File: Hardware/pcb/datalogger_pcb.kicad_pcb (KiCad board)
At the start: 2 copper layers, 127.5 x 123.3 mm, 51 parts, among them J1 Micro_SD_Card_Det2, J2 Switch OUT, SW1 SW_Wuerth_450301014042, SW2 SW_Push, U1 DS3231MZ, U2 SN74LVC2G00DCTR

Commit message: Improvements to PCB and code
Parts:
- 10k: renamed from Pullup CS
- moved 10k 24.2 mm to (156.2, 71.5)
- moved BT1 6.85 mm to (146.7, 95.5)
- moved C4 6.00 mm to (158.5, 82.3)
- moved R5 5.79 mm to (152.2, 84.6), turned to 0 degrees
- moved Rpllup1 2.23 mm to (143.6, 79.0)
- moved Rpllup2 2.10 mm to (147.7, 84.6)
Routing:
- net /Batt+: track 28.3 -> 24.0 mm
- net +3.3V: track 425.5 -> 427.9 mm
- net /I2C0_SCL: track 164.4 -> 162.3 mm
- net Net-(A1-GPIO21): track 130.4 -> 132.2 mm
- net /Data_Onewire: track 95.9 -> 97.2 mm
- net /CS: track 82.1 -> 81.2 mm

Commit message: Small changes
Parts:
- removed RpullupSCL0, RpullupSDA0: 10k, Resistor_THT:R_Axial_DIN0204_L3.6mm_D1.6mm_P5.08mm_Vertical
- renumbered 12V to 12VSWTCH1, 5V to 5VSWTCH1, 10k to RpullupCS1
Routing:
- net /I2C0_SCL: track 162.3 -> 148.3 mm, vias 2 -> 1
- net +3.3V: track 427.9 -> 416.4 mm
- net /I2C0_SDA: track 174.6 -> 170.8 mm

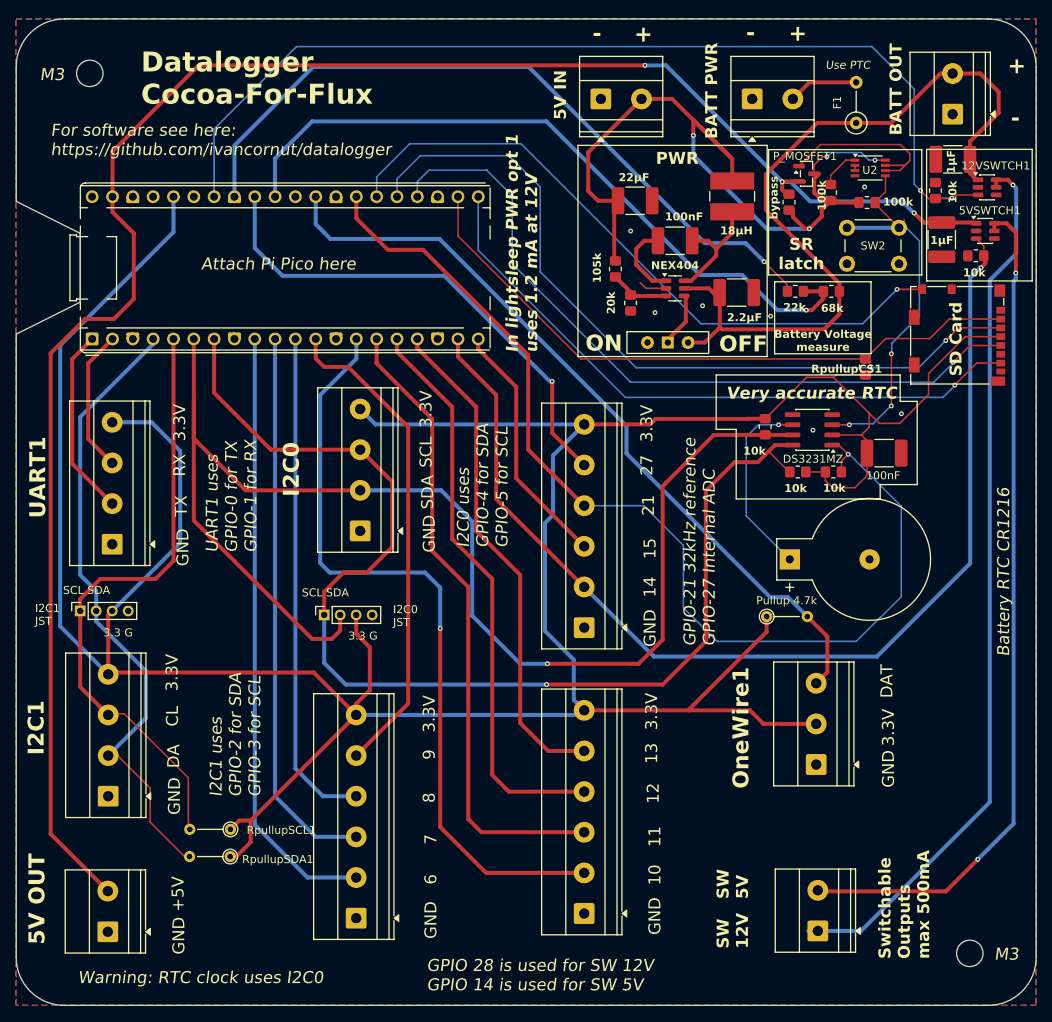
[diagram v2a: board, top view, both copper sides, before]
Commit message: Improved datalogger design and reduced pcb size
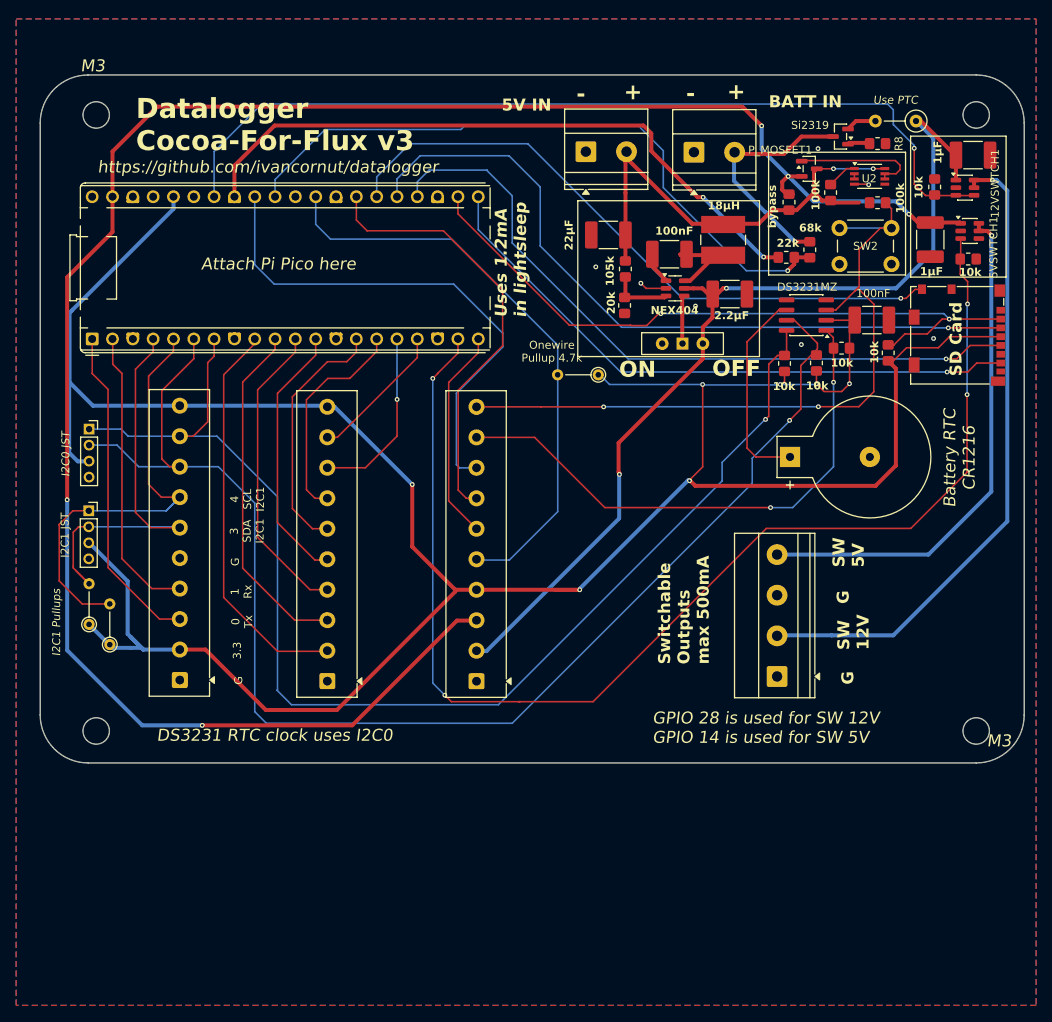
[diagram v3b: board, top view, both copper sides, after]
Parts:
- removed 5VPOUT1: Bornier 5V, TerminalBlock_Phoenix:TerminalBlock_Phoenix_MKDS-1,5-2-5.08_1x02_P5.08mm_Horizontal
- removed GPIO10-1: GPIO10-13, TerminalBlock_Phoenix:TerminalBlock_Phoenix_MKDS-1,5-6-5.08_1x06_P5.08mm_Horizontal
- removed GPIO14-1: GPIO14-17, TerminalBlock_Phoenix:TerminalBlock_Phoenix_MKDS-1,5-6-5.08_1x06_P5.08mm_Horizontal
- removed GPIO6-1: GPIO6-9, TerminalBlock_Phoenix:TerminalBlock_Phoenix_MKDS-1,5-6-5.08_1x06_P5.08mm_Horizontal
- removed I2C0JST1: I2C 0 Connector, Connector_PinSocket_2.00mm:PinSocket_1x04_P2.00mm_Vertical
- removed I2C1: I2C 1 Connector, TerminalBlock_Phoenix:TerminalBlock_Phoenix_MKDS-1,5-4-5.08_1x04_P5.08mm_Horizontal
- removed I2C1JST1: I2C 1 Connector, Connector_PinSocket_2.00mm:PinSocket_1x04_P2.00mm_Vertical
- removed I2C2: I2C 0 Connector, TerminalBlock_Phoenix:TerminalBlock_Phoenix_MKDS-1,5-4-5.08_1x04_P5.08mm_Horizontal
- removed J2: Switch OUT, TerminalBlock_Phoenix:TerminalBlock_Phoenix_MKDS-1,5-2-5.08_1x02_P5.08mm_Horizontal
- removed OneWire1: Connecteur OneWire, TerminalBlock_Phoenix:TerminalBlock_Phoenix_MKDS-1,5-3-5.08_1x03_P5.08mm_Horizontal
- removed PWR12V1: 12V PWR, TerminalBlock_Phoenix:TerminalBlock_Phoenix_MKDS-1,5-2-5.08_1x02_P5.08mm_Horizontal
- removed UART1: UART Connector, TerminalBlock_Phoenix:TerminalBlock_Phoenix_MKDS-1,5-4-5.08_1x04_P5.08mm_Horizontal
- added I2C0 JST: I2C 0 Connector, Connector_PinSocket_2.00mm:PinSocket_1x04_P2.00mm_Vertical, F.Cu at (59.1, 79.3)
- added I2C1 JST: I2C 1 Connector, Connector_PinSocket_2.00mm:PinSocket_1x04_P2.00mm_Vertical, F.Cu at (59.1, 89.5)
- added J3: Conn_01x10_Socket, TerminalBlock_Phoenix:TerminalBlock_Phoenix_MKDS-1-10-3.81_1x10_P3.81mm_Horizontal, F.Cu at (88.9, 110.8)
- added J4: Conn_01x10_Socket, TerminalBlock_Phoenix:TerminalBlock_Phoenix_MKDS-1-10-3.81_1x10_P3.81mm_Horizontal, F.Cu at (107.5, 110.8)
- added J5: Conn_01x10_Socket, TerminalBlock_Phoenix:TerminalBlock_Phoenix_MKDS-1-10-3.81_1x10_P3.81mm_Horizontal, F.Cu at (70.5, 110.6)
- added J6: Conn_01x04_Socket, TerminalBlock_Phoenix:TerminalBlock_Phoenix_MKDS-1,5-4-5.08_1x04_P5.08mm_Horizontal, F.Cu at (145.1, 110.2)
- added Q1: Si2319CDS, Package_TO_SOT_SMD:SOT-23, F.Cu at (153.0, 42.7)
- added R8: 100k, Resistor_SMD:R_0805_2012Metric_Pad1.20x1.40mm_HandSolder, F.Cu at (157.7, 43.6)
- moved Pullup_One_Wire1 36.8 mm to (122.8, 72.5), turned to 180 degrees
- moved RpullupSDA1 34.0 mm to (59.1, 103.7), turned to 90 degrees
- moved RpullupSCL1 27.6 mm to (61.7, 106.2), turned to 90 degrees
- moved C4 16.7 mm to (157.0, 65.6)
- moved R5 15.5 mm to (153.2, 69.2), turned to 180 degrees
- moved U1 14.4 mm to (148.8, 65.0)
- moved Rpllup2 13.7 mm to (146.0, 71.1), turned to 90 degrees
- moved BT1 12.8 mm to (146.7, 82.8)
- moved Rpllup1 10.2 mm to (150.0, 71.0), turned to 90 degrees
- moved PWRIN1 9.87 mm to (134.7, 44.7)
- moved F1 7.48 mm to (162.5, 40.8), turned to 180 degrees
- moved Alim5V1 6.85 mm to (121.2, 44.6)
- moved R1 5.86 mm to (149.2, 56.9), turned to -90 degrees
- moved L_alim1 5.56 mm to (138.4, 55.6)
- moved C3 5.43 mm to (124.0, 55.0), turned to 180 degrees
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- renumbered RpullupCS1 to 10k
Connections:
- F1 pad 2: Net-(PWRIN1-Pin_2) -> Net-(Q1-S)
- PWRIN1 pad 2: Net-(PWRIN1-Pin_2) -> /BATTREAD
- R1 pad 1: +12V -> /BATTREAD
- R5 pad 2: Net-(A1-GPIO21) -> Net-(J4-Pin_9)
- U1 pad 1: Net-(A1-GPIO21) -> Net-(J4-Pin_9)
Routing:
- net +3.3V: track 416.4 -> 334.3 mm, vias 0 -> 7
- net Net-(A1-GPIO21): track 132.2 -> 54.9 mm, vias 1 -> 0
- net Net-(J4-Pin_9): track 0.00 -> 67.8 mm, vias 0 -> 2
- net Net-(A1-GPIO10): track 96.4 -> 31.3 mm, vias 1 -> 0
- net Net-(A1-GPIO11): track 80.0 -> 28.7 mm
- net Net-(A1-GPIO12): track 71.8 -> 22.5 mm, vias 0 -> 1
- net Net-(A1-GPIO13): track 62.8 -> 17.8 mm
- net Net-(5VSWTCH1-QOD): track 106.4 -> 64.9 mm, vias 2 -> 1
- net /RTC_INT: track 48.8 -> 90.0 mm, vias 3 -> 2
- net +5V: track 101.2 -> 61.7 mm, vias 4 -> 2
- net Net-(12VSWTCH1-QOD): track 111.4 -> 81.8 mm
- net /BATTREAD: track 0.00 -> 29.5 mm, vias 0 -> 1
- net Net-(A1-GPIO9): track 61.3 -> 33.2 mm
- net /I2C1_SDA: track 79.5 -> 53.0 mm
- net Net-(A1-GPIO6): track 76.1 -> 49.7 mm
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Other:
- board size 127.5 x 123.3 mm -> 123 x 86 mm
- board text added: "0 Tx"
- board text added: "1 Rx"
- board text added: "3 SDA I2C1"
- board text added: "3.3"
- board text added: "4 SCL I2C1"
- board text added: "BATT IN"
- board text added: "DS3231 RTC clock uses I2C0"
- board text added: "Datalogger Cocoa-For-Flux v3"
- board text added: "G"
- board text added: "I2C1 Pullups"
- board text added: "Onewire Pullup 4.7k"
- board text added: "Si2319"
- board text added: "Uses 1.2mA in lightsleep"
- board text added: "https://github.com/ivancornut/datalogger"
- board text removed: "+5V"
- board text removed: "10"
- board text removed: "11"
- board text removed: "12"
- board text removed: "13"
- board text removed: "14"
- board text removed: "15"
- board text removed: "21"
- board text removed: "27"
- board text removed: "3.3 G"
- board text removed: "3.3V"
- board text removed: "5V OUT"
- board text removed: "6"
- board text removed: "7"
- board text removed: "8"
- board text removed: "9"
- board text removed: "BATT OUT"
- board text removed: "BATT PWR"
- board text removed: "Battery Voltage measure"
- board text removed: "CL"
- board text removed: "DA"
- board text removed: "DAT"
- board text removed: "Datalogger Cocoa-For-Flux"
- board text removed: "For software see here: https://github.com/ivancornut/datalogger"
- board text removed: "GND"
- board text removed: "GPIO-21 32kHz reference GPIO-27 Internal ADC"
- board text removed: "I2C0"
- board text removed: "I2C0 JST"
- board text removed: "I2C0 uses GPIO-4 for SDA GPIO-5 for SCL"
- board text removed: "I2C1 JST"
- board text removed: "I2C1 uses GPIO-2 for SDA GPIO-3 for SCL"
- board text removed: "In lightsleep PWR opt 1 uses 1.2 mA at 12V"
- board text removed: "PWR"
- board text removed: "Pullup 4.7k"
- board text removed: "RX"
- board text removed: "SCL"
- board text removed: "SCL SDA"
- board text removed: "SDA"
- board text removed: "SR latch"
- board text removed: "TX"
- board text removed: "UART1 uses GPIO-0 for TX GPIO-1 for RX"
- board text removed: "Very accurate RTC"
- board text removed: "Warning: RTC clock uses I2C0"

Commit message: Change in pcb picture
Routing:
- net GND: vias 7 -> 8
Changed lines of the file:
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@@
+	)
+	(via
+		(at 72.06 77.93)
+		(size 0.6)
+		(drill 0.3)
+		(layers "F.Cu" "B.Cu")
+		(free yes)
+		(net 32)
 	)
 	(via

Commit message: Made code as retro-compatible as possible
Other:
- board text added: "DS3232MZ"
- board text removed: "DS3231MZ"
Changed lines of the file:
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@@
 		)
 	)
-	(gr_text "DS3231MZ"
+	(gr_text "DS3232MZ"
 		(at 148.88 61.5 0)
 		(layer "F.SilkS")

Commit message: Improvd pcb
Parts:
- moved Pullup_One_Wire1 16.5 mm to (131.7, 86.4), turned to 90 degrees
- moved RpullupSDA1 13.8 mm to (72.4, 99.8)
- moved RpullupSCL1 10.3 mm to (69.8, 99.8)
- moved I2C1 JST 10.3 mm to (68.8, 86.1)
- moved I2C0 JST 9.91 mm to (68.6, 76.5)
- moved J5 8.99 mm to (78.6, 106.8)
- moved J3 8.20 mm to (96.2, 107.0)
- moved A1 7.23 mm to (66.2, 65.3)
- moved J4 6.05 mm to (112.3, 107.0)
- moved Rpllup1 2.89 mm to (147.8, 69.1), turned to 0 degrees
- moved J6 2.56 mm to (145.1, 107.6)
- moved Rpllup2 2.52 mm to (143.8, 72.3), turned to 180 degrees
- moved PWRIN1 2.28 mm to (136.9, 43.9)
- moved R_pullup_shtdwn1 2.12 mm to (155.6, 50.8)
- moved Alim5V1 1.77 mm to (123.0, 44.3)
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- renumbered R8 to 100k
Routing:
- net +3.3V: track 334.3 -> 265.8 mm, vias 7 -> 5
- net +5VP: track 247.6 -> 227.8 mm, vias 5 -> 4
- net /I2C0_SDA: track 170.4 -> 152.8 mm
- net /I2C0_SCL: track 157.5 -> 142.5 mm, vias 1 -> 2
- net /I2C1_SCL: track 57.6 -> 43.8 mm
- net /SCK: track 89.4 -> 78.9 mm, vias 1 -> 2
- net Net-(12VSWTCH1-EN/UVLO): track 112.3 -> 102.4 mm
- net /Data_Onewire: track 73.5 -> 82.8 mm
- net /I2C1_SDA: track 53.0 -> 44.0 mm
- net /AGND: track 82.1 -> 74.0 mm
- net Net-(5VSWTCH1-EN/UVLO): track 153.7 -> 145.7 mm, vias 4 -> 3
- net /CD: track 80.8 -> 73.2 mm
- net /MOSI: track 92.1 -> 84.6 mm
- net GND: track 5.34 -> 12.7 mm, vias 8 -> 3
- net /READ12V: track 83.1 -> 76.0 mm
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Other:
- board size 123 x 86 mm -> 114 x 78 mm
- board text added: "CR1216"
- board text added: "DS3231 RTC: I2C0"
- board text added: "GPIO 28: SW 12V GPIO 14: SW 5V"
- board text removed: "Battery RTC CR1216"
- board text removed: "DS3231 RTC clock uses I2C0"
- board text removed: "GPIO 28 is used for SW 12V GPIO 14 is used for SW 5V"

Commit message: Changes to small pcb
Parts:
- removed P_MOSFET1: Si2319CDS, Package_TO_SOT_SMD:SOT-23
- removed R_BYPASS1: 0 Ohm, Resistor_SMD:R_0805_2012Metric_Pad1.20x1.40mm_HandSolder
- removed R_pullup_int1, R_pullup_shtdwn1: 100k, Resistor_SMD:R_0805_2012Metric_Pad1.20x1.40mm_HandSolder
- removed SW2: SW_Push, Button_Switch_THT:SW_PUSH_6mm_H4.3mm
- removed U2: SN74LVC2G00DCTR, nand:SSOP-8_2.95x2.8mm_P0.65mm - SN74LVC2G00
- I2C0JST1: renamed from I2C0 JST
- I2C1JST1: renamed from I2C1 JST
- moved R8 5.04 mm to (153.8, 46.4), turned to -90 degrees
- renumbered 100k to R8, 10k to RpullupCS1
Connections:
- 5VSWTCH1 pad 1: +5VP -> +5V
- A1 pad 39: +5VP -> +5V
- C6 pad 2: +5VP -> +5V
- J4 pad 3: +5VP -> +5V
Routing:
- net +5VP: track 227.8 -> 0.00 mm, vias 4 -> 0
- net +5V: track 59.4 -> 267.0 mm, vias 2 -> 3
- net /RTC_INT: track 91.0 -> 64.5 mm
- net Net-(P_MOSFET1-G): track 15.8 -> 0.00 mm
- net /READ12V: track 76.0 -> 83.5 mm
- net /SHTDWN_CTRL: track 3.96 -> 0.00 mm
- net GND: track 12.7 -> 10.9 mm, vias 3 -> 2
- net /AGND: track 74.0 -> 73.3 mm
- net Net-(U2-1B): track 0.65 -> 0.00 mm
- net Net-(Q1-G): track 2.96 -> 2.37 mm
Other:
- board size 114 x 78 mm -> 114 x 81 mm
- board text removed: "100k"
